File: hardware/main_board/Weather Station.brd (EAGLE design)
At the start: 64.4 x 77.5 mm, 24 parts, among them J2 RJ12, U1 328P, U2 MCP1703T-3302E/CB, U3 W25X40CLSNIG, X2 B2B-PH-K-S, X3 B2B-XH-2, Y1 8MHz

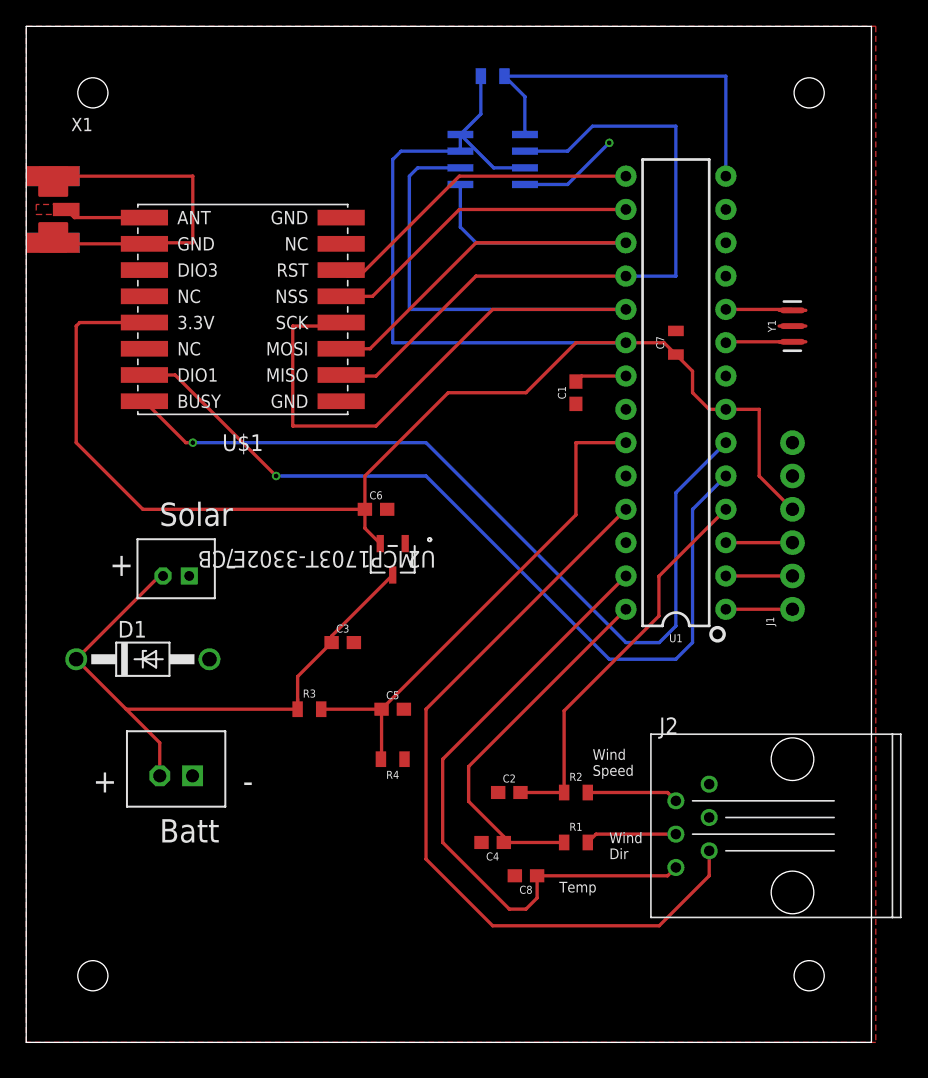
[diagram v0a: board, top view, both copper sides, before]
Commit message: Fixed sleep logic Decreased radio transition times Changed default spreading factor Fixed internal temperature calibration Fixed lack of length prepending weather messages Changed diode for TL431 (TODO: Test unregulated charging, change to PWM if necessary)
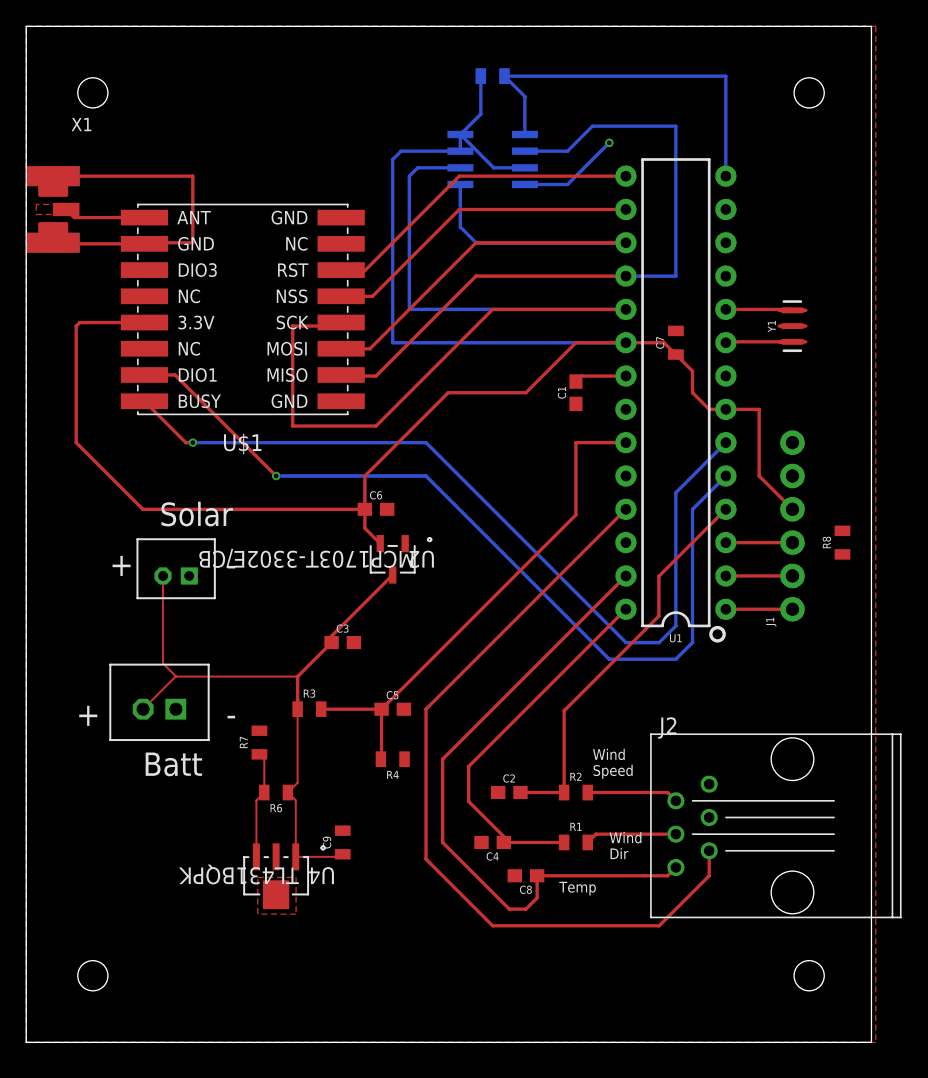
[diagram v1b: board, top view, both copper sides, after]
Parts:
- removed D1: 1N5230BT, diode:DO41Z10
- added C9: 22uF, SparkFun-Capacitors:0805
- added R6, R7, R8: (no value), SparkFun-Resistors:0805
- added U4: TL431BQPK, my-components:PK3
- moved X3 5.24 mm to (10.2, 25.4)
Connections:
- removed net N$9: C3.1, D1.C, R3.1, U2.3, X2.2, X3.2
- new net N$1: R6.2, R7.1, U4.3
- new net VIN: C3.1, C9.1, R3.1, R6.1, U2.3, U4.1, X2.2, X3.2
- net AT_RST: now also R8.1
- net GND: now also C9.2, R7.2, U4.2, U4.A2; no longer D1.A
- net VCC: now also R8.2
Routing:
- net VIN: track 0.00 -> 50.9 mm
- net N$9: track 48.4 -> 0.00 mm
- net N$1: track 0.00 -> 8.21 mm

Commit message: Added wind calibration. Started using namespaces. Added indicator LEDs
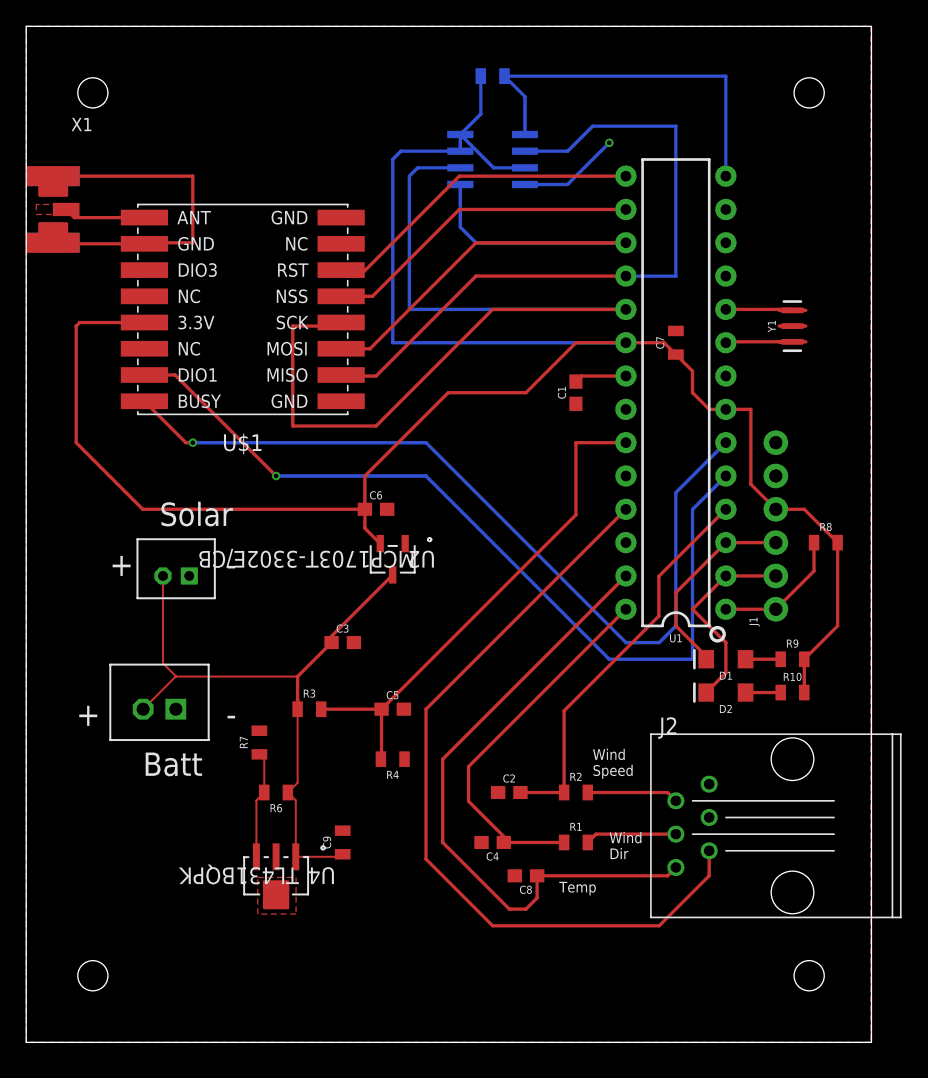
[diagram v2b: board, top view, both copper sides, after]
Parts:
- added D1: RED, SparkFun-LED:LED-1206
- added D2: GREEN, SparkFun-LED:LED-1206
- added R10, R9: (no value), SparkFun-Resistors:0805
- moved J1 1.27 mm to (57.1, 33.0)
- moved R8 1.27 mm to (61.0, 38.1), turned to 0 degrees
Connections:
- new net N$4: D1.A, R9.1
- new net N$6: D2.A, R10.1
- net RX: now also D2.C
- net TX: now also D1.C
- net VCC: now also R10.2, R9.2
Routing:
- net VCC: track 139.5 -> 156.8 mm
- net RX: track 5.08 -> 15.4 mm
- net TX: track 5.08 -> 15.2 mm
- net AT_RST: track 5.08 -> 10.1 mm
- net N$6: track 0.00 -> 2.68 mm
- net N$4: track 0.00 -> 2.68 mm
- net DIO1: track 65.0 -> 65.8 mm
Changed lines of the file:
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@@
 <attribute name="VALUE" x="13.95" y="27.94" size="1.016" layer="27" align="bottom-right"/>
 </element>
-<element name="J1" library="SparkFun-Connectors" library_urn="urn:adsk.eagle:library:513" package="1X06_NO_SILK" package3d_urn="urn:adsk.eagle:package:38130/1" value="" x="58.42" y="33.02" smashed="yes" rot="R90">
-<attribute name="NAME" x="57.023" y="31.75" size="0.6096" layer="25" font="vector" ratio="20" rot="R90"/>
-<attribute name="PROD_ID" value="CONN-08437" x="58.42" y="33.02" size="1.778" layer="27" rot="R90" display="off"/>
-<attribute name="VALUE" x="60.452" y="31.75" size="0.6096" layer="27" font="vector" ratio="20" rot="R90"/>
+<element name="J1" library="SparkFun-Connectors" library_urn="urn:adsk.eagle:library:513" package="1X06_NO_SILK" package3d_urn="urn:adsk.eagle:package:38130/1" value="" x="57.15" y="33.02" smashed="yes" rot="R90">
+<attribute name="NAME" x="55.753" y="31.75" size="0.6096" layer="25" font="vector" ratio="20" rot="R90"/>
+<attribute name="PROD_ID" value="CONN-08437" x="57.15" y="33.02" size="1.778" layer="27" rot="R90" display="off"/>
+<attribute name="VALUE" x="59.182" y="31.75" size="0.6096" layer="27" font="vector" ratio="20" rot="R90"/>
 </element>
 <element name="C7" library="SparkFun-Capacitors" library_urn="urn:adsk.eagle:library:510" package="0805" package3d_urn="urn:adsk.eagle:package:37429/1" value="1.0uF" x="49.53" y="53.34" smashed="yes" rot="R90">
@@
 <attribute name="VALUE" x="25.019" y="15.24" size="0.6096" layer="27" font="vector" ratio="20" rot="R90" align="top-center"/>
 </element>
-<element name="R8" library="SparkFun-Resistors" library_urn="urn:adsk.eagle:library:532" package="0805" package3d_urn="urn:adsk.eagle:package:39651/1" value=" " x="62.23" y="38.1" smashed="yes" rot="R90">
-<attribute name="NAME" x="61.341" y="38.1" size="0.6096" layer="25" font="vector" ratio="20" rot="R90" align="bottom-center"/>
-<attribute name="PROD_ID" value=" " x="62.23" y="38.1" size="1.778" layer="27" rot="R90" display="off"/>
-<attribute name="VALUE" x="63.119" y="38.1" size="0.6096" layer="27" font="vector" ratio="20" rot="R90" align="top-center"/>
+<element name="R8" library="SparkFun-Resistors" library_urn="urn:adsk.eagle:library:532" package="0805" package3d_urn="urn:adsk.eagle:package:39651/1" value=" " x="60.96" y="38.1" smashed="yes">
+<attribute name="NAME" x="60.96" y="38.989" size="0.6096" layer="25" font="vector" ratio="20" align="bottom-center"/>
+<attribute name="PROD_ID" value=" " x="60.96" y="38.1" size="1.778" layer="27" display="off"/>
+<attribute name="VALUE" x="60.96" y="37.211" size="0.6096" layer="27" font="vector" ratio="20" align="top-center"/>
+</element>
+<element name="D1" library="SparkFun-LED" library_urn="urn:adsk.eagle:library:529" package="LED-1206" package3d_urn="urn:adsk.eagle:package:39352/1" value="RED" x="53.34" y="29.21" smashed="yes" rot="R180">
+<attribute name="NAME" x="53.34" y="28.2575" size="0.6096" layer="25" font="vector" ratio="20" rot="R180" align="bottom-center"/>
+<attribute name="PROD_ID" value="DIO-09912" x="53.34" y="29.21" size="1.778" layer="27" rot="R180" display="off"/>
+<attribute name="VALUE" x="53.34" y="30.1625" size="0.6096" layer="27" font="vector" ratio="20" rot="R180" align="top-center"/>
+</element>
+<element name="D2" library="SparkFun-LED" library_urn="urn:adsk.eagle:library:529" package="LED-1206" package3d_urn="urn:adsk.eagle:package:39352/1" value="GREEN" x="53.34" y="26.67" smashed="yes" rot="R180">
+<attribute name="NAME" x="53.34" y="25.7175" size="0.6096" layer="25" font="vector" ratio="20" rot="R180" align="bottom-center"/>
+<attribute name="PROD_ID" value="DIO-00862" x="53.34" y="26.67" size="1.778" layer="27" rot="R180" display="off"/>
+<attribute name="VALUE" x="53.34" y="27.6225" size="0.6096" layer="27" font="vector" ratio="20" rot="R180" align="top-center"/>
+</element>
+<element name="R9" library="SparkFun-Resistors" library_urn="urn:adsk.eagle:library:532" package="0805" package3d_urn="urn:adsk.eagle:package:39651/1" value=" " x="58.42" y="29.21" smashed="yes">
+<attribute name="NAME" x="58.42" y="30.099" size="0.6096" layer="25" font="vector" ratio="20" align="bottom-center"/>
+<attribute name="PROD_ID" value=" " x="58.42" y="29.21" size="1.778" layer="27" display="off"/>
+<attribute name="VALUE" x="58.42" y="28.321" size="0.6096" layer="27" font="vector" ratio="20" align="top-center"/>
+</element>
+<element name="R10" library="SparkFun-Resistors" library_urn="urn:adsk.eagle:library:532" package="0805" package3d_urn="urn:adsk.eagle:package:39651/1" value=" " x="58.42" y="26.67" smashed="yes">
+<attribute name="NAME" x="58.42" y="27.559" size="0.6096" layer="25" font="vector" ratio="20" align="bottom-center"/>
+<attribute name="PROD_ID" value=" " x="58.42" y="26.67" size="1.778" layer="27" display="off"/>
+<attribute name="VALUE" x="58.42" y="25.781" size="0.6096" layer="27" font="vector" ratio="20" align="top-center"/>
 </element>
 </elements>
@@
 <polygon width="0.1524" layer="1" isolate="0.3048">
 <vertex x="0" y="77.47"/>
-<vertex x="64.77" y="77.47"/>
-<vertex x="64.77" y="0"/>
+<vertex x="64.389" y="77.47"/>
+<vertex x="64.389" y="0"/>
 <vertex x="0" y="0"/>
 </polygon>
@@
 <wire x1="50.8" y1="49.53" x2="52.07" y2="48.26" width="0.254" layer="1"/>
 <wire x1="52.07" y1="48.26" x2="53.34" y2="48.26" width="0.254" layer="1"/>
-<wire x1="53.34" y1="48.26" x2="55.88" y2="48.26" width="0.254" layer="1"/>
-<wire x1="55.88" y1="48.26" x2="55.88" y2="43.18" width="0.254" layer="1"/>
-<wire x1="55.88" y1="43.18" x2="58.42" y2="40.64" width="0.254" layer="1"/>
+<wire x1="53.34" y1="48.26" x2="55.245" y2="48.26" width="0.254" layer="1"/>
+<wire x1="55.245" y1="48.26" x2="55.245" y2="42.545" width="0.254" layer="1"/>
+<wire x1="55.245" y1="42.545" x2="57.15" y2="40.64" width="0.254" layer="1"/>
 <wire x1="41.91" y1="53.34" x2="38.1" y2="49.53" width="0.254" layer="1"/>
 <wire x1="41.91" y1="53.34" x2="45.72" y2="53.34" width="0.254" layer="1"/>
@@
 <wire x1="25.82" y1="39.1952" x2="26.99" y2="38.0252" width="0.254" layer="1"/>
 <contactref element="R8" pad="2"/>
-<wire x1="58.42" y1="40.64" x2="62.23" y2="39" width="0" layer="19" extent="1-1"/>
+<contactref element="R10" pad="2"/>
+<contactref element="R9" pad="2"/>
+<wire x1="57.15" y1="40.64" x2="59.32" y2="40.64" width="0.254" layer="1"/>
+<wire x1="59.32" y1="40.64" x2="61.86" y2="38.1" width="0.254" layer="1"/>
+<wire x1="61.86" y1="38.1" x2="61.86" y2="31.75" width="0.254" layer="1"/>
+<wire x1="61.86" y1="31.75" x2="59.32" y2="29.21" width="0.254" layer="1"/>
+<wire x1="59.32" y1="29.21" x2="59.32" y2="26.67" width="0.254" layer="1"/>
 </signal>
 <signal name="MISO">
@@
 <wire x1="19.05" y1="43.18" x2="30.48" y2="43.18" width="0.254" layer="16"/>
 <wire x1="30.48" y1="43.18" x2="44.45" y2="29.21" width="0.254" layer="16"/>
-<wire x1="44.45" y1="29.21" x2="49.53" y2="29.21" width="0.254" layer="16"/>
-<wire x1="49.53" y1="29.21" x2="50.8" y2="30.48" width="0.254" layer="16"/>
-<wire x1="50.8" y1="30.48" x2="50.8" y2="40.64" width="0.254" layer="16"/>
+<wire x1="44.45" y1="29.21" x2="50.8" y2="29.21" width="0.254" layer="16"/>
+<wire x1="50.8" y1="29.21" x2="50.8" y2="40.64" width="0.254" layer="16"/>
 <wire x1="50.8" y1="40.64" x2="53.34" y2="43.18" width="0.254" layer="16"/>
 </signal>
@@
 <contactref element="U1" pad="2"/>
 <contactref element="J1" pad="2"/>
-<wire x1="53.34" y1="35.56" x2="58.42" y2="35.56" width="0.254" layer="1"/>
+<wire x1="53.34" y1="35.56" x2="57.15" y2="35.56" width="0.254" layer="1"/>
+<contactref element="D2" pad="C"/>
+<wire x1="51.84" y1="26.67" x2="53.34" y2="28.17" width="0.254" layer="1"/>
+<wire x1="53.34" y1="28.17" x2="53.34" y2="30.48" width="0.254" layer="1"/>
+<wire x1="53.34" y1="30.48" x2="50.8" y2="33.02" width="0.254" layer="1"/>
+<wire x1="50.8" y1="33.02" x2="53.34" y2="35.56" width="0.254" layer="1"/>
 </signal>
 <signal name="TX">
 <contactref element="U1" pad="3"/>
 <contactref element="J1" pad="3"/>
-<wire x1="53.34" y1="38.1" x2="58.42" y2="38.1" width="0.254" layer="1"/>
+<wire x1="53.34" y1="38.1" x2="57.15" y2="38.1" width="0.254" layer="1"/>
+<contactref element="D1" pad="C"/>
+<wire x1="51.84" y1="29.21" x2="51.84" y2="29.44" width="0.1524" layer="1"/>
+<wire x1="51.84" y1="29.44" x2="49.53" y2="31.75" width="0.254" layer="1"/>
+<wire x1="49.53" y1="31.75" x2="49.53" y2="34.29" width="0.254" layer="1"/>
+<wire x1="49.53" y1="34.29" x2="53.34" y2="38.1" width="0.254" layer="1"/>
 </signal>
 <signal name="AT_RST">
 <contactref element="U1" pad="1"/>
 <contactref element="J1" pad="1"/>
-<wire x1="53.34" y1="33.02" x2="58.42" y2="33.02" width="0.254" layer="1"/>
+<wire x1="53.34" y1="33.02" x2="57.15" y2="33.02" width="0.254" layer="1"/>
 <contactref element="R8" pad="1"/>
-<wire x1="58.42" y1="33.02" x2="62.23" y2="37.2" width="0" layer="19" extent="1-1"/>
+<wire x1="57.15" y1="33.02" x2="60.06" y2="35.93" width="0.254" layer="1"/>
+<wire x1="60.06" y1="35.93" x2="60.06" y2="38.1" width="0.254" layer="1"/>
 </signal>
 <signal name="WINDDIR_PWR">
@@
 <wire x1="17.55" y1="18.45" x2="18.15" y2="19.05" width="0.1524" layer="1"/>
 </signal>
+<signal name="N$4">
+<contactref element="D1" pad="A"/>
+<contactref element="R9" pad="1"/>
+<wire x1="54.84" y1="29.21" x2="57.52" y2="29.21" width="0.254" layer="1"/>
+</signal>
+<signal name="N$6">
+<contactref element="D2" pad="A"/>
+<contactref element="R10" pad="1"/>
+<wire x1="54.84" y1="26.67" x2="57.52" y2="26.67" width="0.254" layer="1"/>
+</signal>
 </signals>

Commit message: Added PWM charge control circuitry
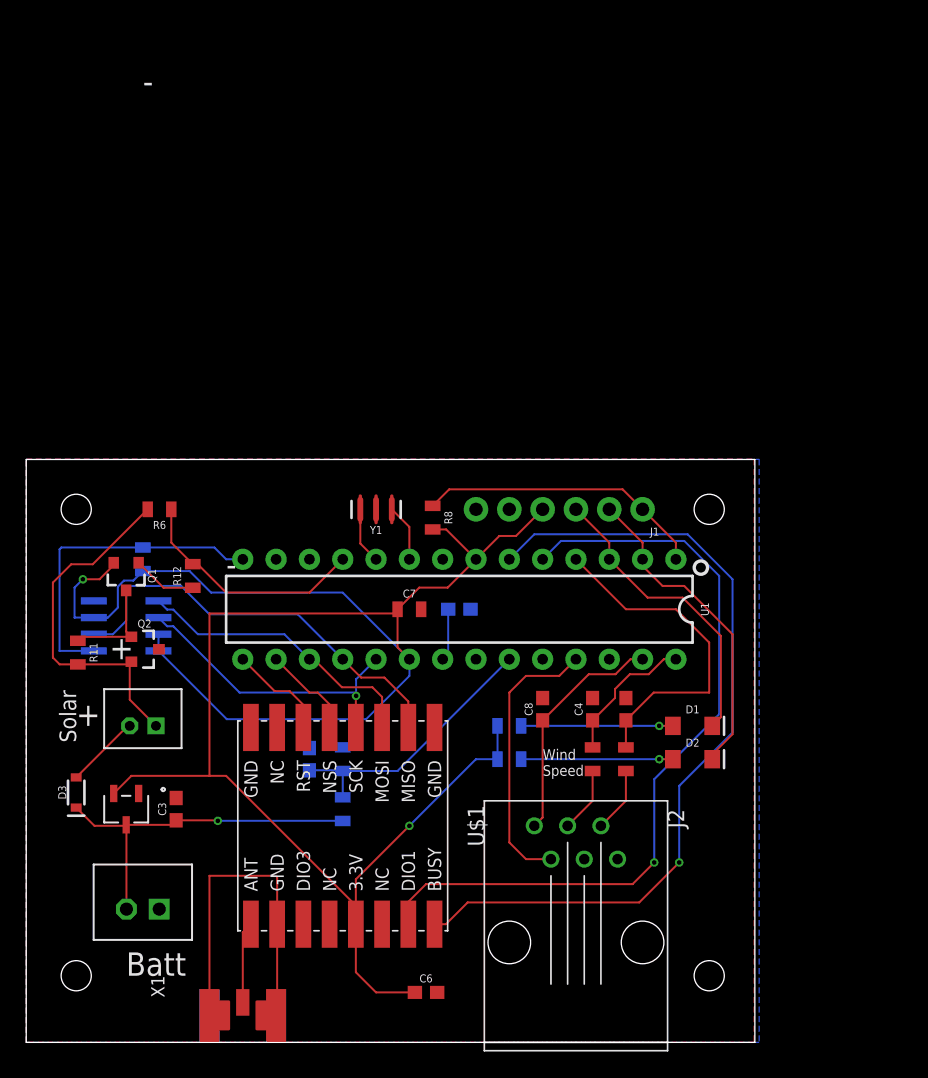
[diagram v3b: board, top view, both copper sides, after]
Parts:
- removed C9: 22uF, SparkFun-Capacitors:0805
- removed R7: (no value), SparkFun-Resistors:0805
- removed U4: TL431BQPK, my-components:PK3
- added D3: 0.5A/40V/420mV, SparkFun-DiscreteSemi:SOD-323
- added Q1: 200mA/40V, SparkFun-DiscreteSemi:SOT23-3
- added Q2: 220mA/50V/3.5Ω, SparkFun-DiscreteSemi:SOT23-3
- added R11: 33k, SparkFun-Resistors:0805
- added R12: 1k, SparkFun-Resistors:0805
- R6: value (none) -> 100k
- moved X1 65.6 mm to (16.5, 0.00), turned to 90 degrees
- moved R5 45.5 mm to (8.89, 36.8), turned to 90 degrees
- moved U3 45.2 mm to (7.62, 31.8), turned to 180 degrees
- moved U$1 40.1 mm to (24.1, 16.5), turned to 270 degrees
- moved C6 37.0 mm to (30.5, 3.81)
- moved Y1 34.7 mm to (26.7, 40.6), turned to 180 degrees
- moved R8 30.0 mm to (31.0, 40.0), turned to 270 degrees
- moved C7 28.7 mm to (29.2, 33.0), turned to 0 degrees
- moved U2 27.9 mm to (7.62, 17.8)
- moved R6 23.3 mm to (10.2, 40.6)
- moved U1 23.3 mm to (33.0, 33.0), turned to 180 degrees
- moved R10 22.2 mm to (36.8, 21.6), flipped to the bottom
- moved R9 22.2 mm to (36.8, 24.1), flipped to the bottom
- moved J2 18.8 mm to (41.9, 7.62), turned to 270 degrees
- moved C1 18.8 mm to (33.0, 33.0), flipped to the bottom, turned to 0 degrees
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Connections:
- removed net N$1: R6.2, R7.1, U4.3
- new net N$12: Q1.3, Q2.1, R11.1
- new net N$13: Q1.1, R12.1
- new net N$14: D3.A, X2.2
- new net N$9: Q2.2, R11.2, R6.2, X2.1
- new net PWM_SOLAR: R12.2, R6.1, U1.11
- net GND: now also Q2.3; no longer C9.2, R7.2, U4.2, U4.A2, X2.1
- net VCC: now also Q1.2
- net VIN: now also D3.C; no longer C9.1, R6.1, U4.1, X2.2
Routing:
- net SCK: track 71.3 -> 23.3 mm, vias 0 -> 1
- net WINDDIR_PWR: track 60.2 -> 21.3 mm
- net TEMP_SENSE: track 48.3 -> 17.9 mm
- net N$9: track 0.00 -> 27.2 mm
- net VIN: track 50.9 -> 27.5 mm, vias 0 -> 1
- net MISO: track 52.4 -> 32.7 mm
- net MOSI: track 41.4 -> 22.4 mm
- net PWM_SOLAR: track 0.00 -> 18.2 mm
- net BATT_SENSE: track 38.7 -> 20.8 mm
- net WINDDIR_SENSE: track 28.5 -> 10.7 mm
- net SX_RST: track 25.1 -> 7.78 mm
- net SX_NSS: track 24.5 -> 7.26 mm
- net AT_RST: track 10.1 -> 22.0 mm
- net VCC: track 156.8 -> 166.0 mm, vias 0 -> 2
- net RX: track 15.4 -> 24.6 mm
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- added copper zone on layer 16, net GND
- removed copper zone on layer 1, net ANT
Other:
- board size 64.4 x 77.5 mm -> 55.5 x 44.4 mm
- board text removed: "Temp"
- board text removed: "Wind Dir"
- board text removed: "Wind Power"
